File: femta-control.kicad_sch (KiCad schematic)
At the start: 45 parts, among them J1 CUBESAT INTERFACE, U1 NCV1117-12_SOT223, U2 MAX6103, U3 MCP3208

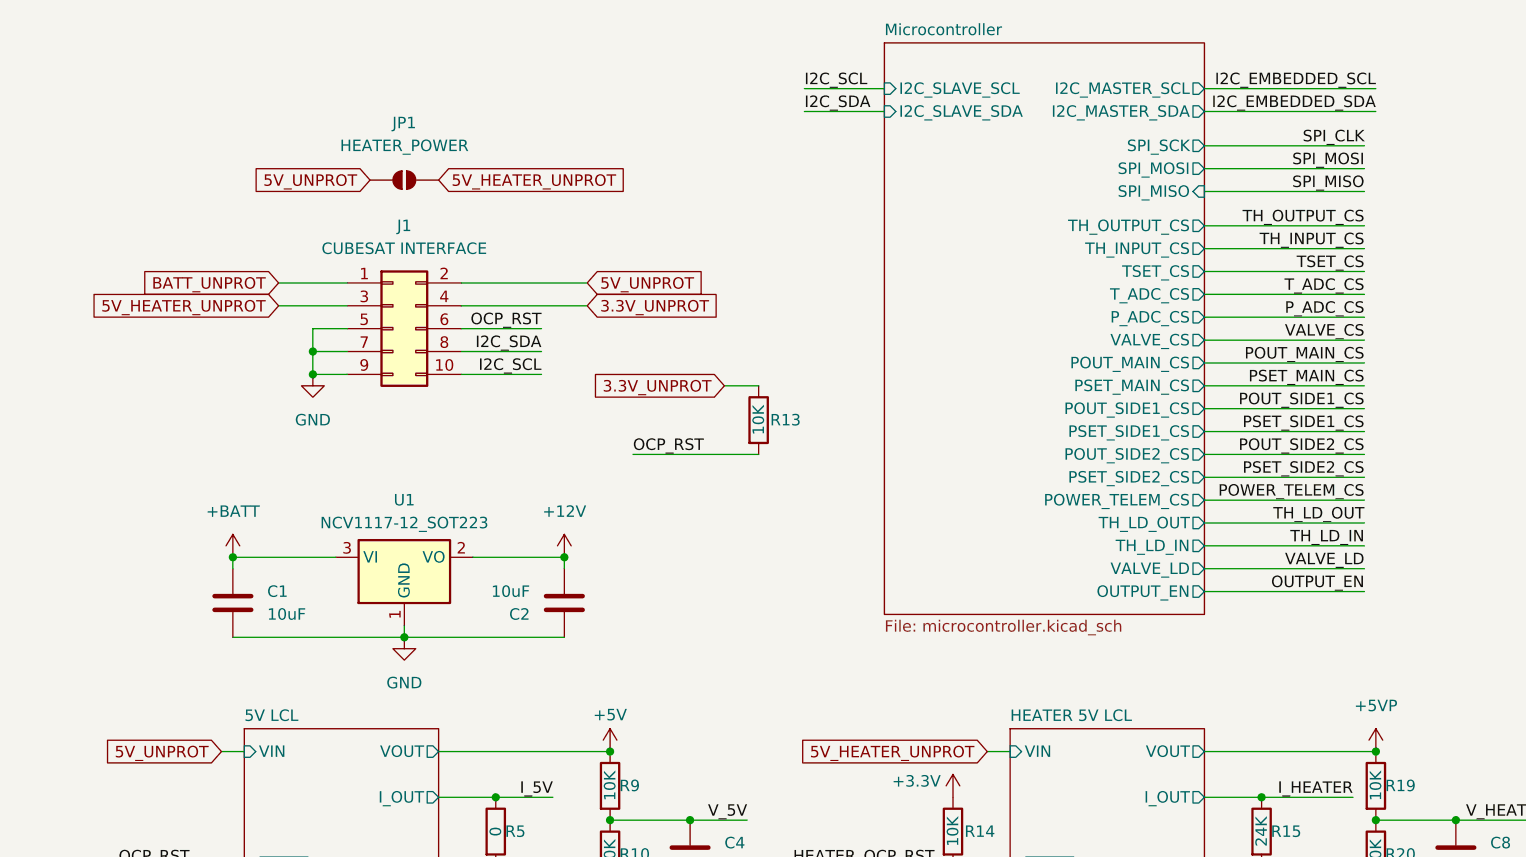
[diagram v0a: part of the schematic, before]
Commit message: ocp reset connect and esd protection
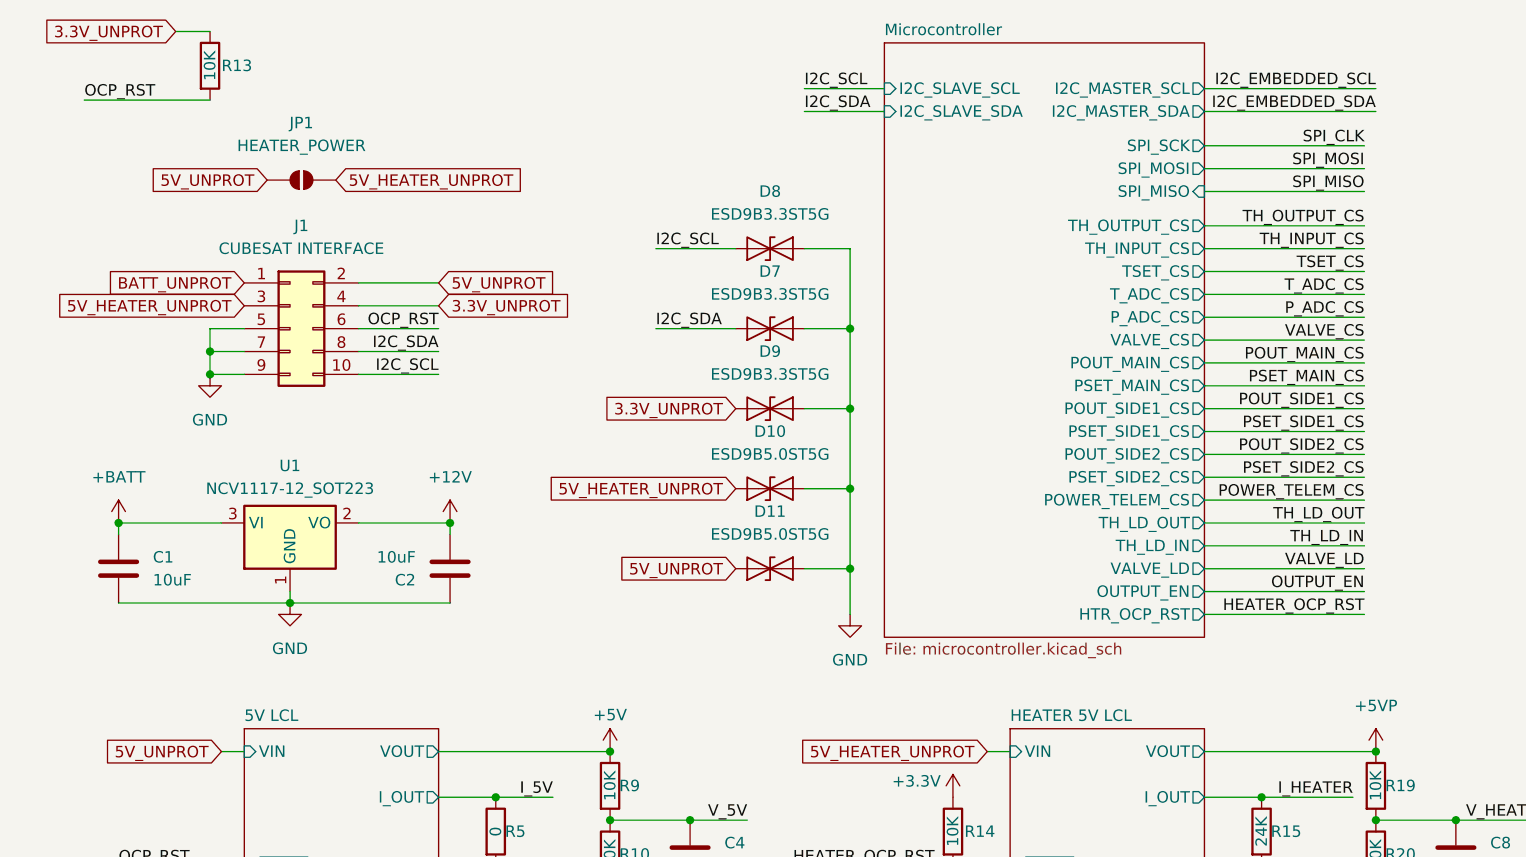
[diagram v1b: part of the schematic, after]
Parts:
- added D10, D11: ESD9B5.0ST5G, Diode_SMD:D_SOD-923, symbol Diode:ESD9B5.0ST5G
- added D7, D8, D9: ESD9B3.3ST5G, Diode_SMD:D_SOD-923, symbol Diode:ESD9B3.3ST5G
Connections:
- net 3.3V_UNPROT: now also D9.1 (A1)
- net 5V_HEATER_UNPROT: now also D10.1 (A1)
- net 5V_UNPROT: now also D11.1 (A1)
- net GND: now also D10.2 (A2), D11.2 (A2), D7.2 (A2), D8.2 (A2), D9.2 (A2)
- net I2C_SCL: now also D8.1 (A1)
- net I2C_SDA: now also D7.1 (A1)
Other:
- sheet Microcontroller ports: added HTR_OCP_RST; removed none
- moved on the sheet: C1, C2, J1, JP1, R13, U1

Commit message: footprint selection
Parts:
- JP1: footprint (none) -> Jumper:SolderJumper-2_P1.3mm_Open_RoundedPad1.0x1.5mm
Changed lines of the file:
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@@
 			)
 		)
-		(property "Footprint" ""
+		(property "Footprint" "Jumper:SolderJumper-2_P1.3mm_Open_RoundedPad1.0x1.5mm"
 			(at 44.45 31.75 0)
 			(effects
